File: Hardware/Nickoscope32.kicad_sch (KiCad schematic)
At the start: 0 parts

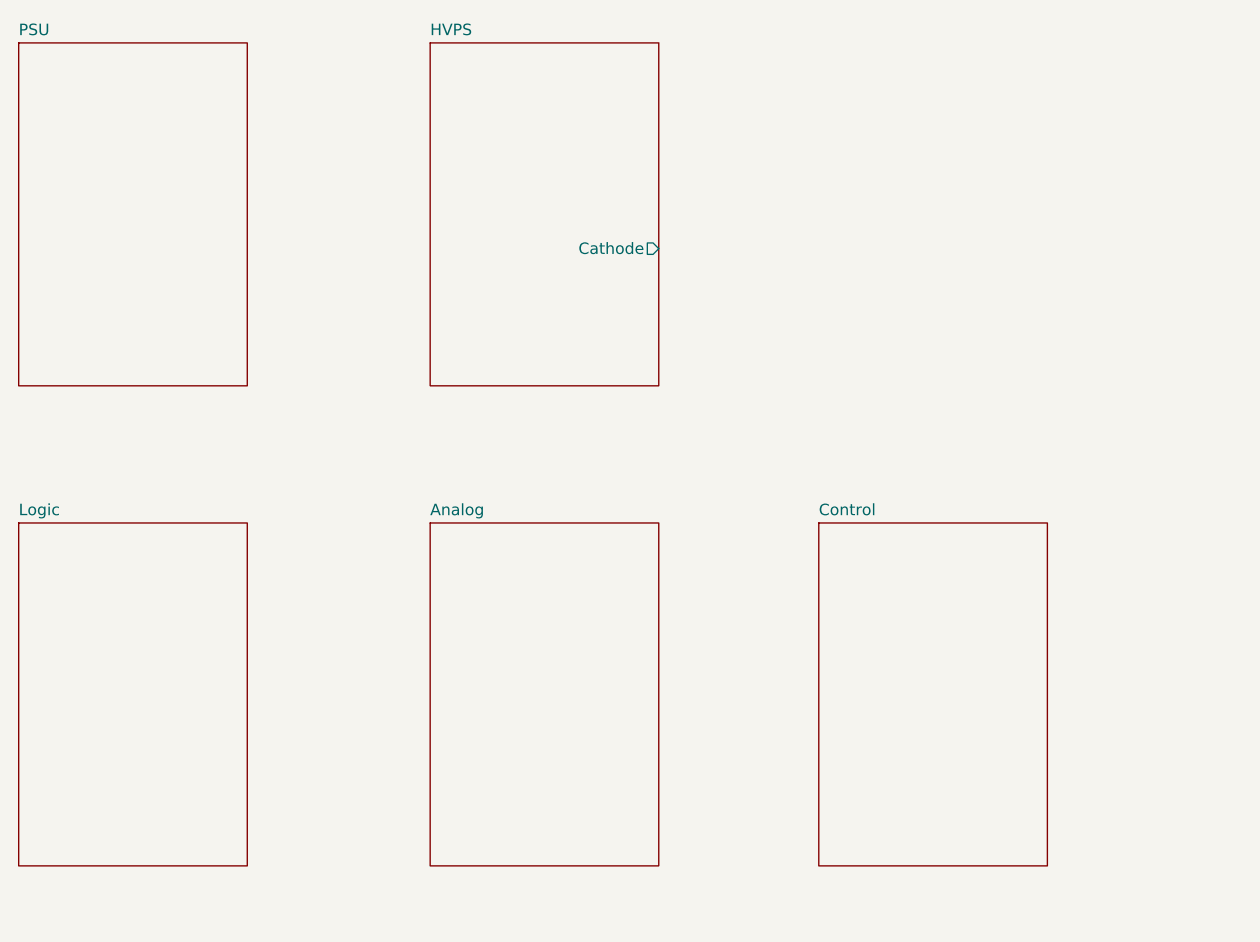
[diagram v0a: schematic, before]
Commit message: Added scheme of logic board
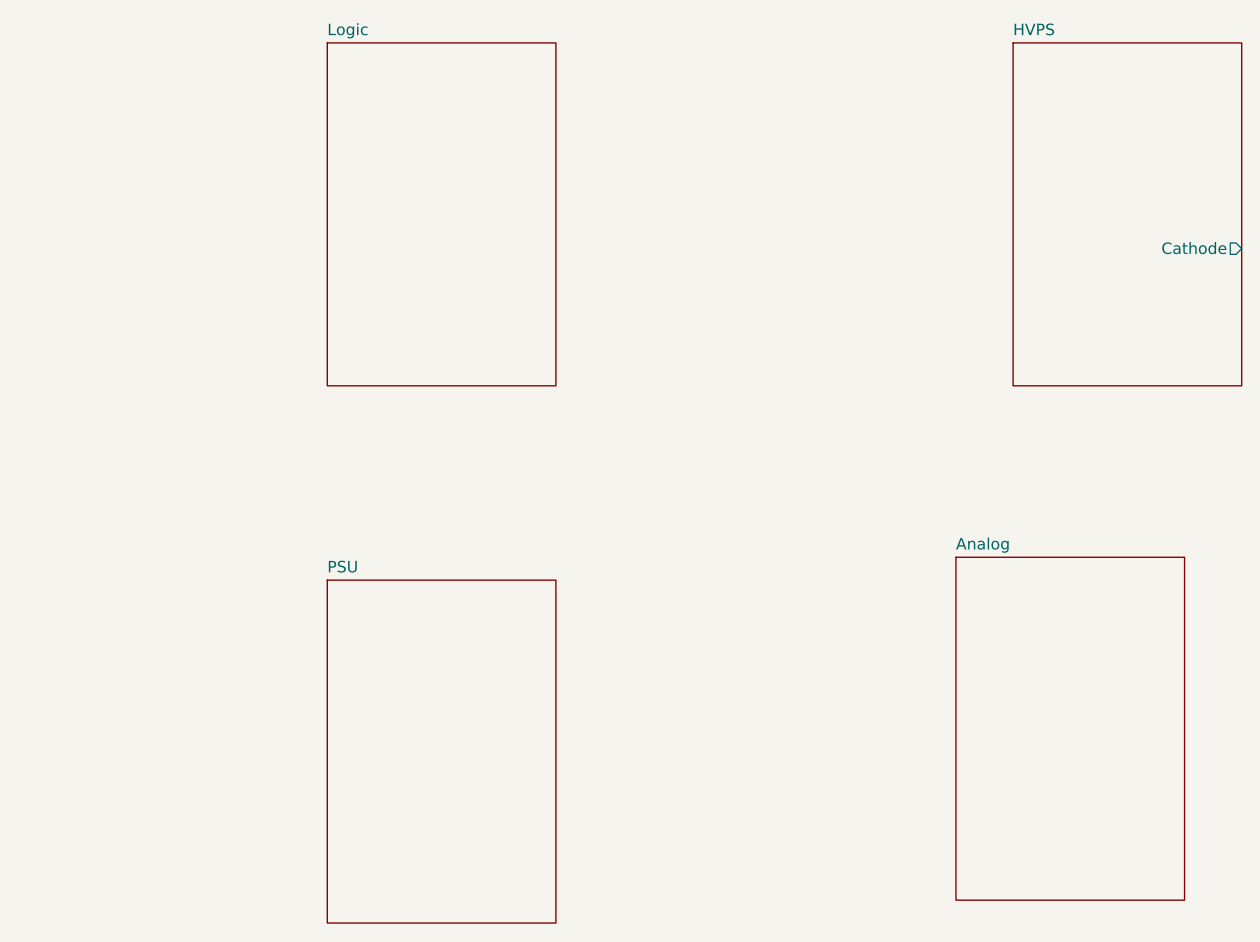
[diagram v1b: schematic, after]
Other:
- removed sheet Control
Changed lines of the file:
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@@
 	(title_block
 		(title "Nickoscope32")
+		(date "2026/04/01")
 		(rev "0.1")
 	)
 	(sheet
-		(at 55.88 101.6)
+		(at 90.17 161.29)
 		(size 25.4 38.1)
 		(exclude_from_sim no)
@@
 		)
 		(property "Sheetname" "PSU"
-			(at 55.88 100.8884 0)
+			(at 90.17 160.5784 0)
 			(show_name no)
 			(do_not_autoplace no)
@@
 		)
 		(property "Sheetfile" "./PSU/PSU.kicad_sch"
-			(at 55.88 140.2846 0)
+			(at 90.17 199.9746 0)
 			(hide yes)
 			(show_name no)
@@
 	)
 	(sheet
-		(at 55.88 154.94)
+		(at 160.02 158.75)
+		(size 25.4 38.1)
+		(exclude_from_sim no)
+		(in_bom yes)
+		(on_board yes)
+		(dnp no)
+		(fields_autoplaced yes)
+		(stroke
+			(width 0.1524)
+			(type solid)
+		)
+		(fill
+			(color 0 0 0 0)
+		)
+		(property "Sheetname" "Analog"
+			(at 160.02 158.0384 0)
+			(show_name no)
+			(do_not_autoplace no)
+			(effects
+				(font
+					(size 1.27 1.27)
+				)
+				(justify left bottom)
+			)
+		)
+		(property "Sheetfile" "./Analog/Analog.kicad_sch"
+			(at 160.02 197.4346 0)
+			(hide yes)
+			(show_name no)
+			(do_not_autoplace no)
+			(effects
+				(font
+					(size 1.27 1.27)
+				)
+				(justify left top)
+			)
+		)
+		(instances
+			(project "Nickoscope32"
+				(path "/657a6403-bab3-4845-b291-93bf2a64f630"
+					(page "5")
+				)
+			)
+		)
+	)
+	(sheet
+		(at 90.17 101.6)
 		(size 25.4 38.1)
 		(exclude_from_sim no)
@@
 		)
 		(property "Sheetname" "Logic"
-			(at 55.88 154.2284 0)
+			(at 90.17 100.8884 0)
 			(show_name no)
 			(do_not_autoplace no)
@@
 		)
 		(property "Sheetfile" "./Logic/Logic.kicad_sch"
-			(at 55.88 193.6246 0)
+			(at 90.17 140.2846 0)
 			(hide yes)
 			(show_name no)
@@
 	)
 	(sheet
-		(at 101.6 101.6)
+		(at 166.37 101.6)
 		(size 25.4 38.1)
 		(exclude_from_sim no)
@@
 		)
 		(property "Sheetname" "HVPS"
-			(at 101.6 100.8884 0)
+			(at 166.37 100.8884 0)
 			(show_name no)
 			(do_not_autoplace no)
@@
 		)
 		(property "Sheetfile" "./HVPS/HVPS.kicad_sch"
-			(at 101.6 140.2846 0)
+			(at 166.37 140.2846 0)
 			(hide yes)
 			(show_name no)
@@
 		)
 		(pin "Cathode" output
-			(at 127 124.46 0)
+			(at 191.77 124.46 0)
 			(effects
 				(font
@@
 				)
 			)
-		)
-	)
-	(sheet
-		(at 144.78 154.94)
-		(size 25.4 38.1)
-		(exclude_from_sim no)
-		(in_bom yes)
-		(on_board yes)
-		(dnp no)
-		(fields_autoplaced yes)
-		(stroke
-			(width 0.1524)
-			(type solid)
-		)
-		(fill
-			(color 0 0 0 0)
-		)
-		(property "Sheetname" "Control"
-			(at 144.78 154.2284 0)
-			(show_name no)
-			(do_not_autoplace no)
-			(effects
-				(font
-					(size 1.27 1.27)
-				)
-				(justify left bottom)
-			)
-		)
-		(property "Sheetfile" ".\\Control\\Control.kicad_sch"
-			(at 144.78 193.6246 0)
-			(hide yes)
-			(show_name no)
-			(do_not_autoplace no)
-			(effects
-				(font
-					(size 1.27 1.27)
-				)
-				(justify left top)
-			)
-		)
-		(instances
-			(project "Nickoscope32"
-				(path "/657a6403-bab3-4845-b291-93bf2a64f630"
-					(page "6")
-				)
-			)
-		)
-	)
-	(sheet
-		(at 101.6 154.94)
-		(size 25.4 38.1)
-		(exclude_from_sim no)
-		(in_bom yes)
-		(on_board yes)
-		(dnp no)
-		(fields_autoplaced yes)
-		(stroke
-			(width 0.1524)
-			(type solid)
-		)
-		(fill
-			(color 0 0 0 0)
-		)
-		(property "Sheetname" "Analog"
-			(at 101.6 154.2284 0)
-			(show_name no)
-			(do_not_autoplace no)
-			(effects
-				(font
-					(size 1.27 1.27)
-				)
-				(justify left bottom)
-			)
-		)
-		(property "Sheetfile" "./Analog/Analog.kicad_sch"
-			(at 101.6 193.6246 0)
-			(hide yes)
-			(show_name no)
-			(do_not_autoplace no)
-			(effects
-				(font
-					(size 1.27 1.27)
-				)
-				(justify left top)
-			)
-		)
-		(instances
-			(project "Nickoscope32"
-				(path "/657a6403-bab3-4845-b291-93bf2a64f630"
-					(page "5")
-				)
-			)
